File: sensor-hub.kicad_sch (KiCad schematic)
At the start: 8 parts, among them J2 Screw_Terminal_01x08, SW1 SW_SPDT, SW2 SW_SPST, U1 MCP23017_SP

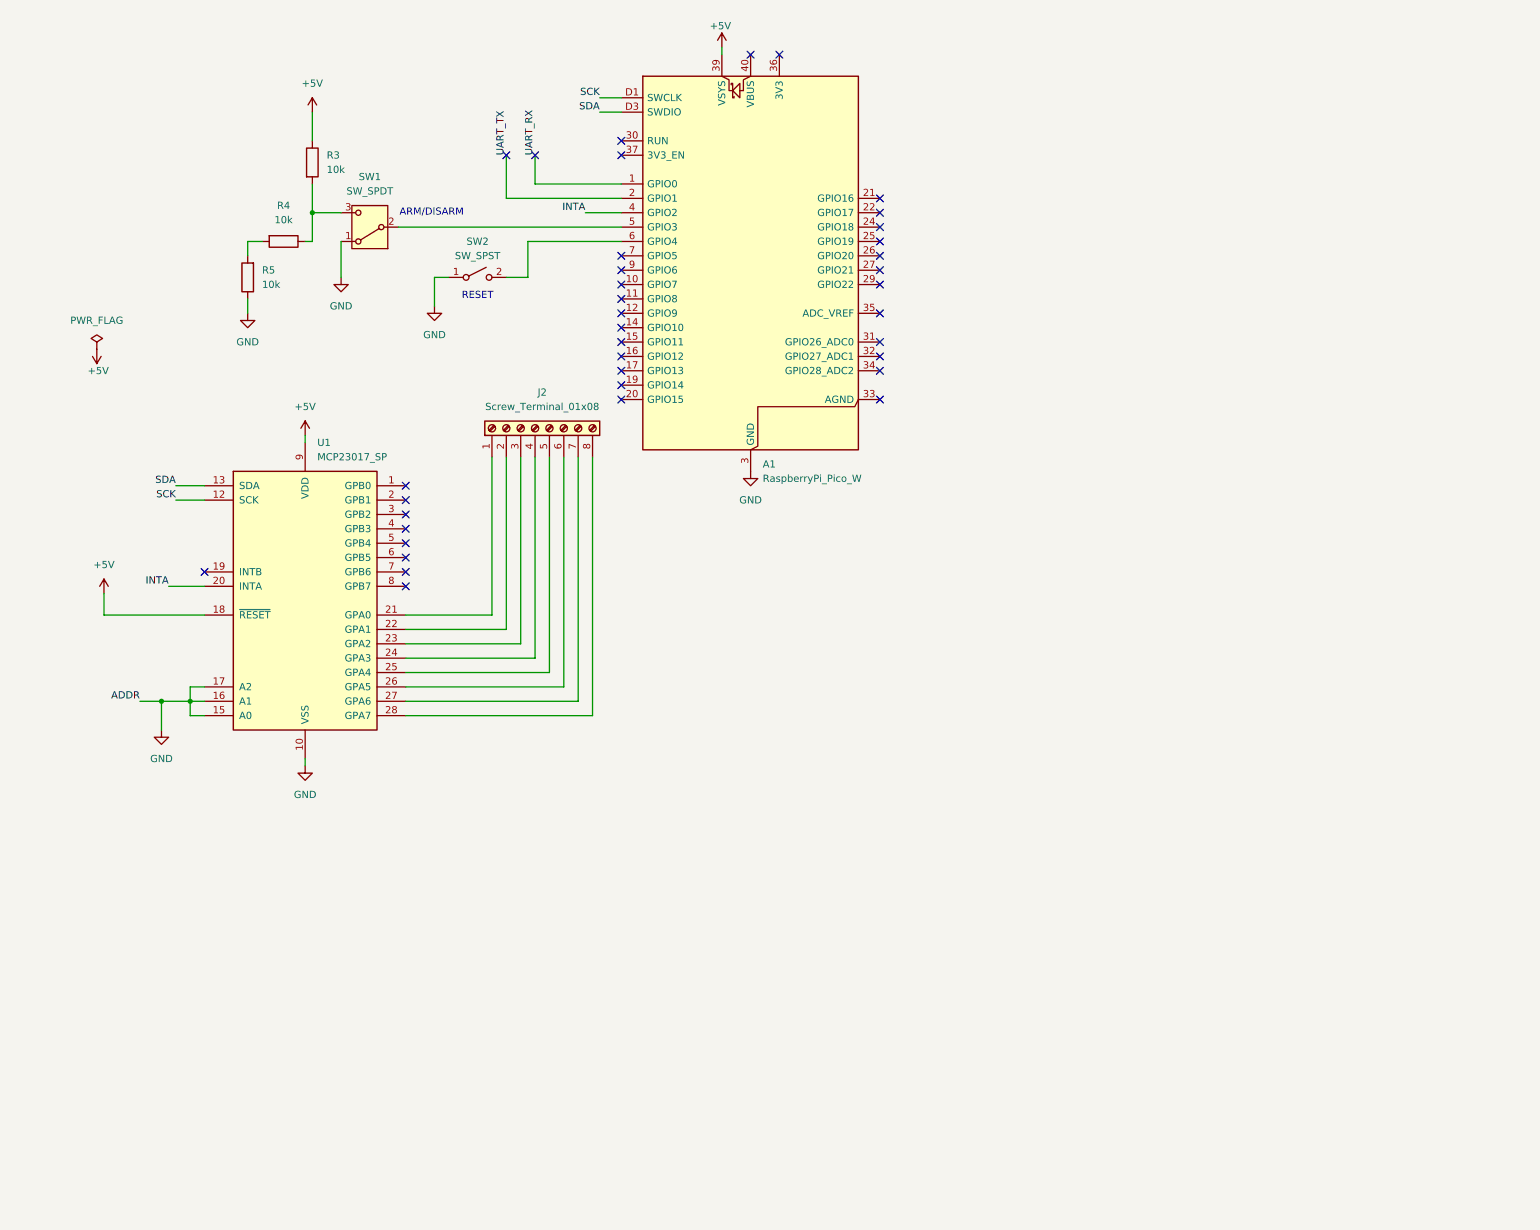
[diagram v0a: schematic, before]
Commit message: power good leds, buzzer control, other minor stuff for convenience
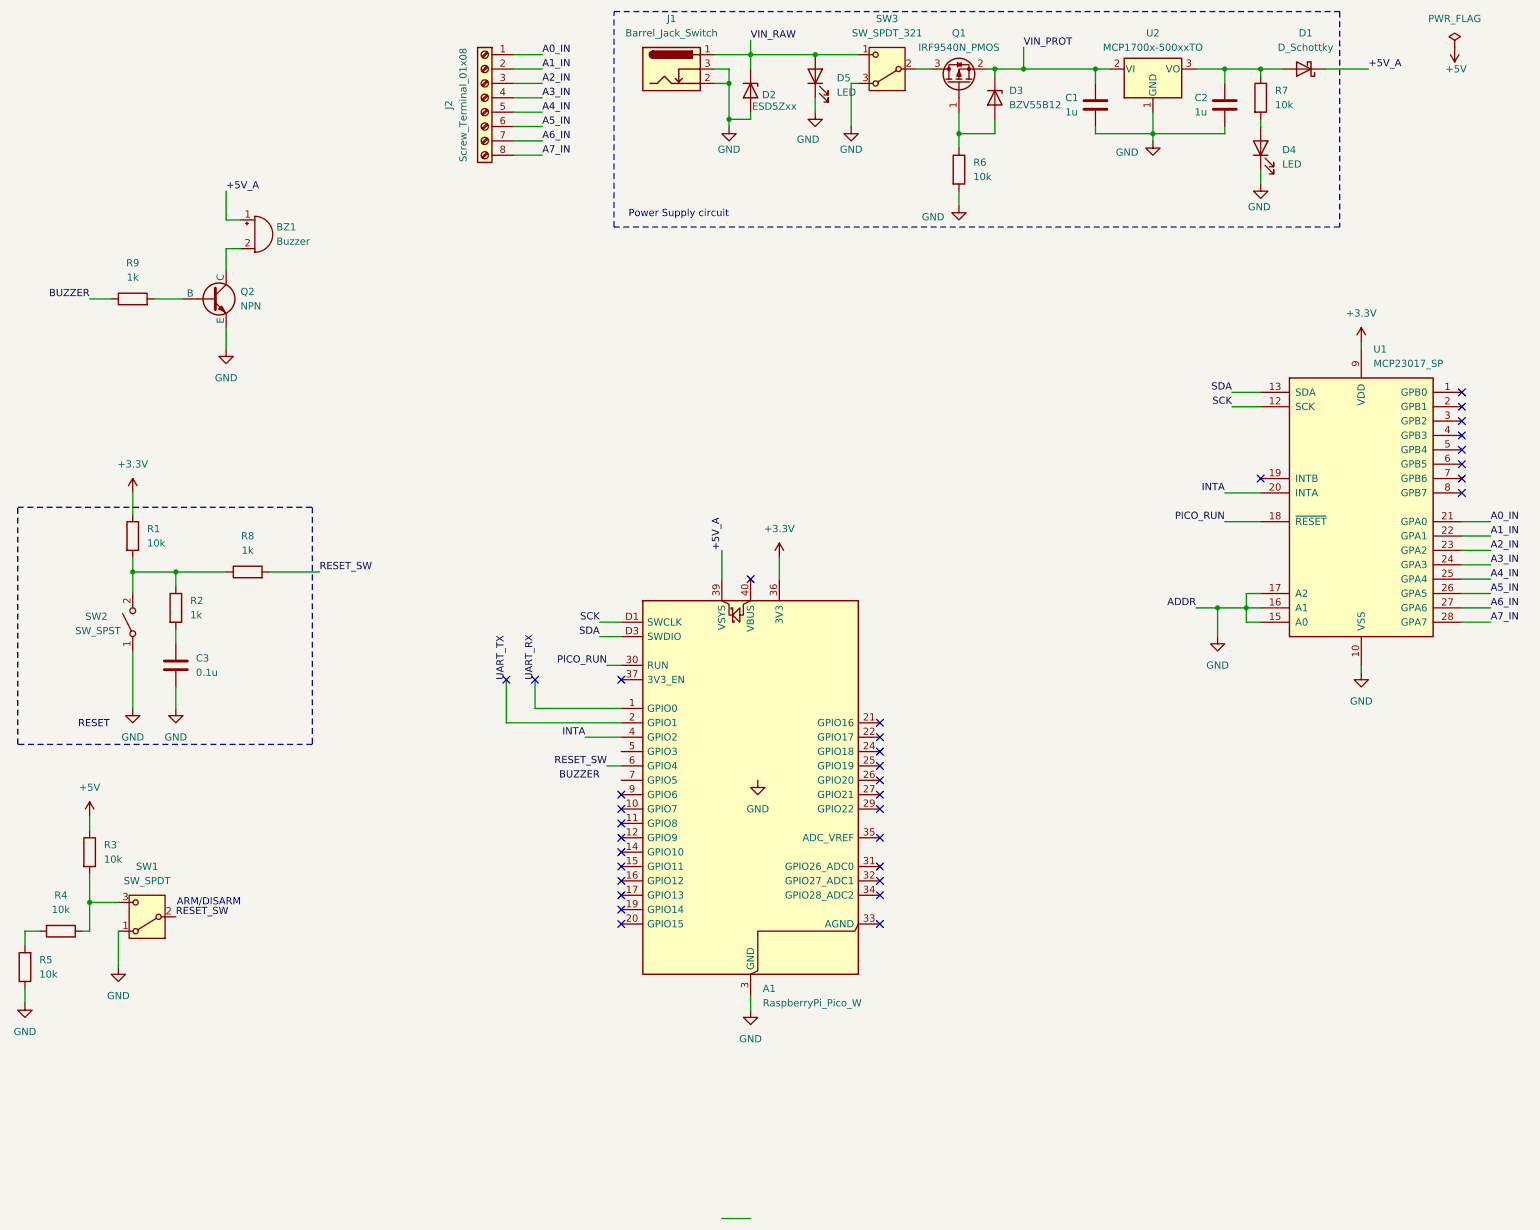
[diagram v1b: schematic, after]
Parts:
- added BZ1: Buzzer, symbol Device:Buzzer
- added C1, C2: 1u, Capacitor_THT:CP_Radial_D10.0mm_P2.50mm, symbol Device:C
- added C3: 0.1u, Capacitor_THT:CP_Radial_D10.0mm_P2.50mm, symbol Device:C
- added D1: D_Schottky, Diode_THT:D_DO-15_P2.54mm_Vertical_AnodeUp, symbol Device:D_Schottky
- added D2: ESD5Zxx, Diode_SMD:D_SOD-523, symbol Diode:ESD5Zxx
- added D3: BZV55B12, Diode_SMD:D_MiniMELF, symbol Diode:BZV55B12
- added D4, D5: LED, symbol Device:LED
- added J1: Barrel_Jack_Switch, Connector_BarrelJack:BarrelJack_Horizontal, symbol Connector:Barrel_Jack_Switch
- added Q1: IRF9540N_PMOS, symbol Transistor_FET:Q_PMOS_GSD
- added Q2: NPN, symbol Simulation_SPICE:NPN
- added R1, R6, R7: 10k, Resistor_THT:R_Axial_DIN0207_L6.3mm_D2.5mm_P2.54mm_Vertical, symbol Device:R
- added R2, R8, R9: 1k, Resistor_THT:R_Axial_DIN0207_L6.3mm_D2.5mm_P2.54mm_Vertical, symbol Device:R
- added SW3: SW_SPDT_321, symbol Switch:SW_SPDT_321
- added U2: MCP1700x-500xxTO, Package_TO_SOT_THT:TO-92_Inline, symbol Regulator_Linear:MCP1700x-500xxTO
- A1: footprint Module:RaspberryPi_Pico_W_SMD_HandSolder -> Module:RaspberryPi_Pico_Common_THT
- J2: footprint (none) -> TerminalBlock_Phoenix:TerminalBlock_Phoenix_PT-1,5-8-3.5-H_1x08_P3.50mm_Horizontal
- R3, R4, R5: footprint (none) -> Resistor_THT:R_Axial_DIN0207_L6.3mm_D2.5mm_P2.54mm_Vertical
- SW1: footprint (none) -> Button_Switch_THT:SW_Slide-03_Wuerth-WS-SLTV_10x2.5x6.4_P2.54mm
- SW2: footprint (none) -> Button_Switch_THT:SW_PUSH-12mm_Wuerth-430476085716
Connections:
- net +5V: no longer A1.39 (VSYS), U1.18 (~{RESET}), U1.9 (VDD)
- net GND: now also C1.2, C2.2, C3.2, D2.2 (A), D4.1 (K), D5.1 (K), J1.2, J1.3, Q2.3 (E), R6.2, SW3.3 (A), U2.1 (GND)
- net A0_IN: now reaches J2.1 (Pin_1), U1.21 (GPA0)
- net A1_IN: now reaches J2.2 (Pin_2), U1.22 (GPA1)
- net A2_IN: now reaches J2.3 (Pin_3), U1.23 (GPA2)
- net A3_IN: now reaches J2.4 (Pin_4), U1.24 (GPA3)
- net A4_IN: now reaches J2.5 (Pin_5), U1.25 (GPA4)
- net A5_IN: now reaches J2.6 (Pin_6), U1.26 (GPA5)
- net A6_IN: now reaches J2.7 (Pin_7), U1.27 (GPA6)
- net A7_IN: now reaches J2.8 (Pin_8), U1.28 (GPA7)
- net PICO_RUN: now reaches A1.30 (RUN)
- net PICO_RUN: now also U1.18 (~{RESET})
- net +3.3V: now reaches A1.36 (3V3)
- net +3.3V: now also U1.9 (VDD), R1.1
- net at A1.5 (GPIO3): no longer SW1.2 (B)
- net at SW2.2 (B): now also R1.2, R2.1, R8.1; no longer A1.6 (GPIO4)
- new net: D3.2 (A), Q1.1 (G), R6.1
- new net: Q1.3 (D), SW3.2 (B)
- new net: BZ1.2 (-), Q2.1 (C)
- new net: Q2.2 (B), R9.2
- new net: D4.2 (A), R7.2
- new net: C2.1, D1.2 (A), R7.1, U2.3 (VO)
- new net: C3.1, R2.2
- new net +5V_A: A1.39 (VSYS), BZ1.1 (+), D1.1 (K)
- new net BUZZER: R9.1
- new net RESET_SW: A1.6 (GPIO4), R8.2, SW1.2 (B)
- new net VIN_PROT: C1.1, D3.1 (K), Q1.2 (S), U2.2 (VI)
- new net VIN_RAW: D2.1 (K), D5.2 (A), J1.1, SW3.1 (C)
- no-connect marks 38 -> 35
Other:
- note added: "Power Supply circuit"
- moved on the sheet: A1, J2, R3, R4, R5, SW1, SW2, U1
